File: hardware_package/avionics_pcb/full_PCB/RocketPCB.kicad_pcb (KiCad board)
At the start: 2 copper layers, 0.8 x 1 mm, 72 parts, among them J1 DX07S024XJ1R1100, J2 Micro_SD_Card, J3 Conn_01x03_Female, M1 Motor_Servo_JR, M2 Motor_Servo_JR, Q1 DMG2301L, Q2 DMG2301L, SW1 SW_Push, SW2 SW_Push, U1 STM32F405RGTx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

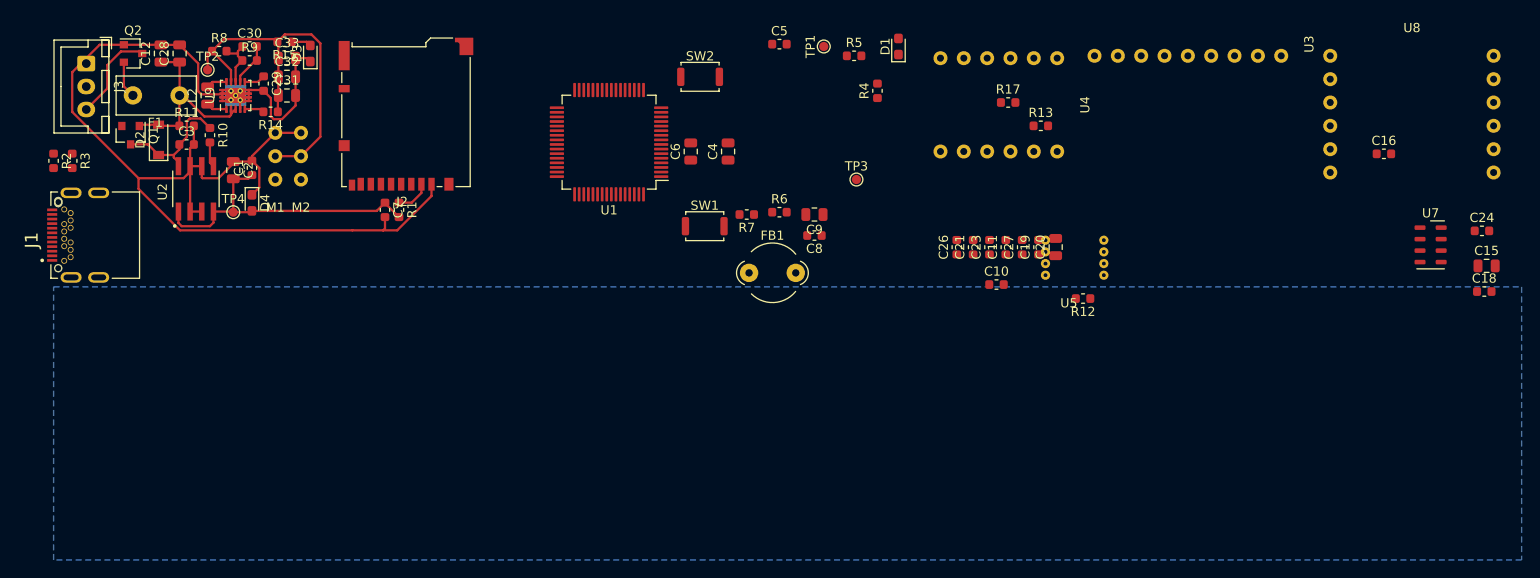
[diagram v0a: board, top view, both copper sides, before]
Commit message: Laid out and routed the majority of the board
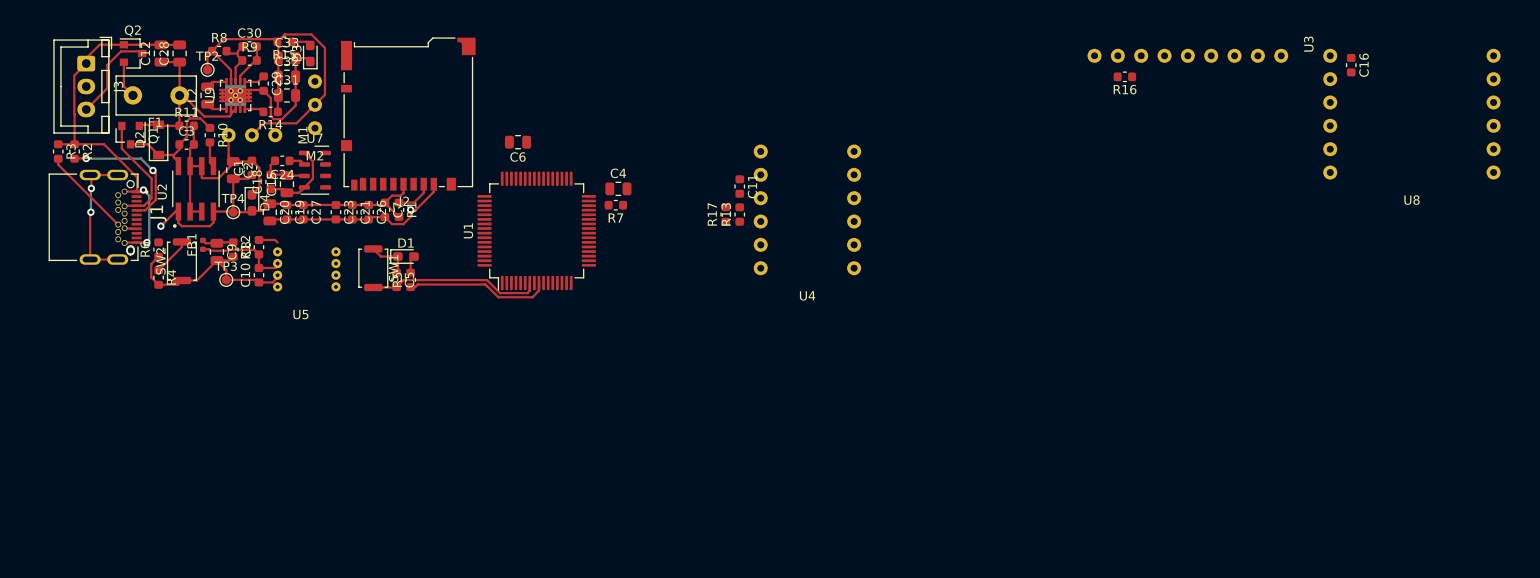
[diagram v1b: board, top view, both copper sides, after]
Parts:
- removed TP1: TestPoint, TestPoint:TestPoint_Pad_D1.0mm
- added R16: 4.7K, Resistor_SMD:R_0603_1608Metric, F.Cu at (182.6, 59.9)
- C7: value C -> 100nF
- FB1: footprint Ferrite_THT:LairdTech_28C0236-0JW-10 -> Resistor_SMD:R_0402_1005Metric
- moved C18 132.6 mm to (89.7, 71.4), turned to 90 degrees
- moved C15 130.9 mm to (91.4, 71.6), turned to 90 degrees
- moved C24 130.8 mm to (90.9, 69.1), turned to 180 degrees
- moved U7 121.7 mm to (94.5, 70.1)
- moved R12 89.9 mm to (88.4, 78.5), turned to 90 degrees
- moved C20 85.6 mm to (89.6, 74.7), turned to 270 degrees
- moved U5 83.6 mm to (93.0, 85.3)
- moved C19 81.9 mm to (91.4, 74.7), turned to 270 degrees
- moved R4 80.8 mm to (77.5, 81.8), turned to 270 degrees
- moved C10 80.3 mm to (88.4, 81.5), turned to 90 degrees
- moved C27 78.3 mm to (93.2, 74.7), turned to 270 degrees
- moved C23 71.2 mm to (96.8, 74.7), turned to 270 degrees
- moved TP3 69.4 mm to (84.8, 82.0)
- moved R6 67.7 mm to (77.5, 78.7), turned to 90 degrees
- moved C21 67.7 mm to (98.6, 74.7), turned to 270 degrees
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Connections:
- net /A0 renamed Net-(U1-Pad20)
- net /CLKIN renamed Net-(U4-Pad8)
- U1 pad 16: /PPS -> Net-(U1-Pad16)
- U1 pad 21: /INT2 -> Net-(U1-Pad21)
- U1 pad 22: /INT1 -> Net-(U1-Pad22)
- U1 pad 23: /INT -> Net-(U1-Pad23)
- U1 pad 26: /CS -> Net-(U1-Pad26)
- U1 pad 39: /SDIO_D0 -> /SDIO_D1
- U1 pad 40: /SDIO_D1 -> /SDIO_D0
- U3 pad 8: /CS -> Net-(R16-Pad2)
- U4 pad 6: /INT -> Net-(U4-Pad6)
- U7 pad 5: /INT2 -> Net-(U7-Pad5)
- U7 pad 6: /INT1 -> Net-(U7-Pad6)
- U8 pad 11: /PPS -> Net-(U8-Pad11)
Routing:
- net +3V3: track 33.7 -> 68.7 mm, vias 0 -> 1
- net ~RESET~: track 0.00 -> 18.9 mm
- net /D13: track 0.00 -> 15.8 mm
- net Net-(J1-PadS1): track 0.00 -> 15.3 mm, vias 0 -> 2
- net Net-(J1-PadA5): track 0.00 -> 15.0 mm, vias 0 -> 2
- net VBUS: track 0.00 -> 13.8 mm
- net GND: track 139.4 -> 149.4 mm, vias 0 -> 3
- net Net-(J1-PadB5): track 0.00 -> 9.87 mm
- net /BOOT0: track 0.00 -> 4.14 mm
- net Net-(C8-Pad1): track 0.00 -> 3.47 mm
- net /FLASH_CS: track 0.00 -> 2.15 mm
- net Net-(D1-Pad2): track 0.00 -> 1.90 mm
- net Net-(C24-Pad1): track 0.00 -> 1.78 mm
- added copper zone on PWR, net +3V3
- added copper zone on GND, net GND
- removed copper zone on B.Cu, net GND
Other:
- copper layers 2 -> 4

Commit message: Continued routing pins, 18 left
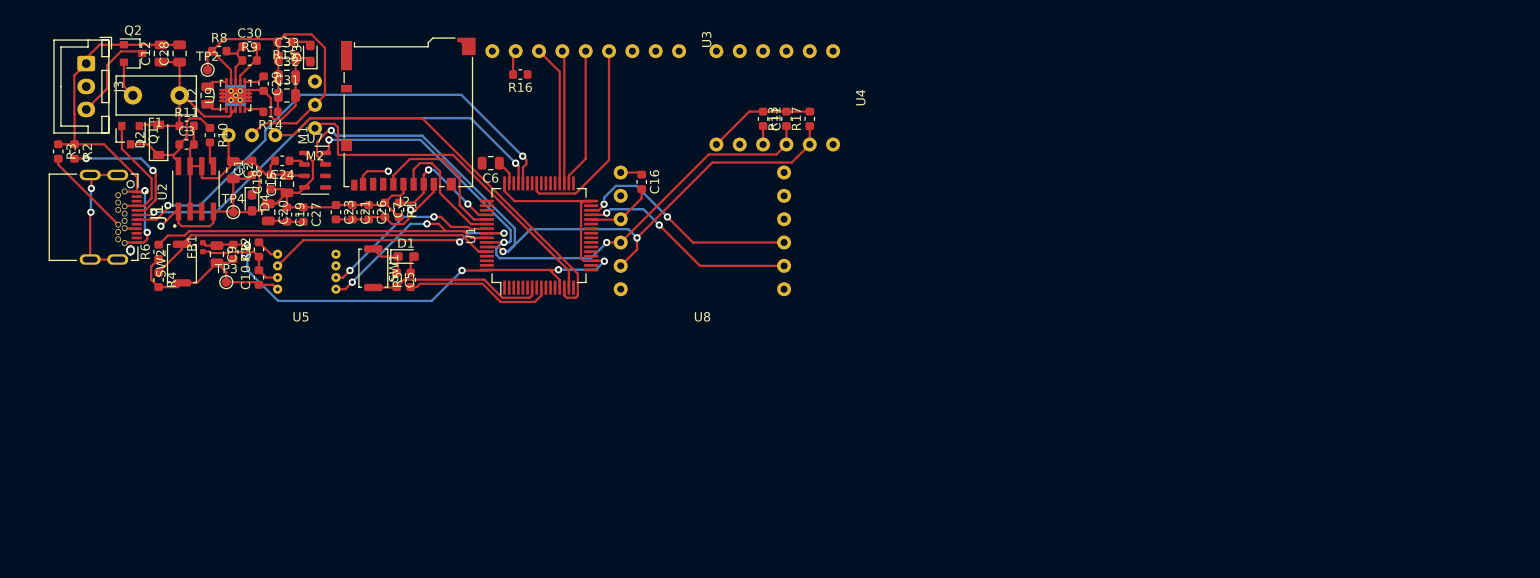
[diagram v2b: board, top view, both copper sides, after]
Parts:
- removed C4: 10uF, Capacitor_SMD:C_0805_2012Metric
- removed R7: 100k, Resistor_SMD:R_0603_1608Metric
- moved C16 78.3 mm to (130.0, 71.4)
- moved U8 78.3 mm to (136.7, 84.3)
- moved R16 65.8 mm to (116.8, 59.7)
- moved U3 65.5 mm to (135.4, 57.1)
- moved U4 21.7 mm to (153.4, 62.2), turned to 90 degrees
- moved R17 13.9 mm to (148.3, 64.5)
- moved R13 11.6 mm to (145.8, 64.5)
- moved C11 7.79 mm to (143.3, 64.5)
- moved C6 3.75 mm to (113.6, 69.3)
- moved U1 0.57 mm to (118.9, 77.2)
- moved C19 0.25 mm to (91.4, 74.9)
- moved C27 0.25 mm to (93.2, 74.9)
- moved C8 0.25 mm to (85.6, 79.0)
- moved C9 0.25 mm to (83.8, 79.2)
- moved FB1 0.25 mm to (82.3, 78.5)
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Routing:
- net /SDA: track 0.00 -> 78.8 mm, vias 0 -> 3
- net /SCL: track 0.00 -> 69.9 mm, vias 0 -> 3
- net Net-(C8-Pad1): track 3.47 -> 72.7 mm, vias 0 -> 4
- net /D-: track 0.00 -> 54.5 mm, vias 0 -> 2
- net /FLASH_MOSI: track 0.00 -> 51.9 mm, vias 0 -> 2
- net /D+: track 0.00 -> 50.0 mm, vias 0 -> 2
- net /PWM0: track 0.00 -> 45.6 mm
- net /PWM1: track 0.00 -> 38.0 mm
- net /BOOT0: track 4.14 -> 38.5 mm
- net /FLASH_MISO: track 0.00 -> 28.1 mm, vias 0 -> 2
- net /RX_D0: track 0.00 -> 25.1 mm, vias 0 -> 2
- net /TX_D1: track 0.00 -> 23.8 mm, vias 0 -> 2
- net /G0: track 0.00 -> 22.2 mm
- net /FLASH_SCK: track 0.00 -> 19.7 mm, vias 0 -> 2
- net +3V3: track 68.7 -> 85.3 mm
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
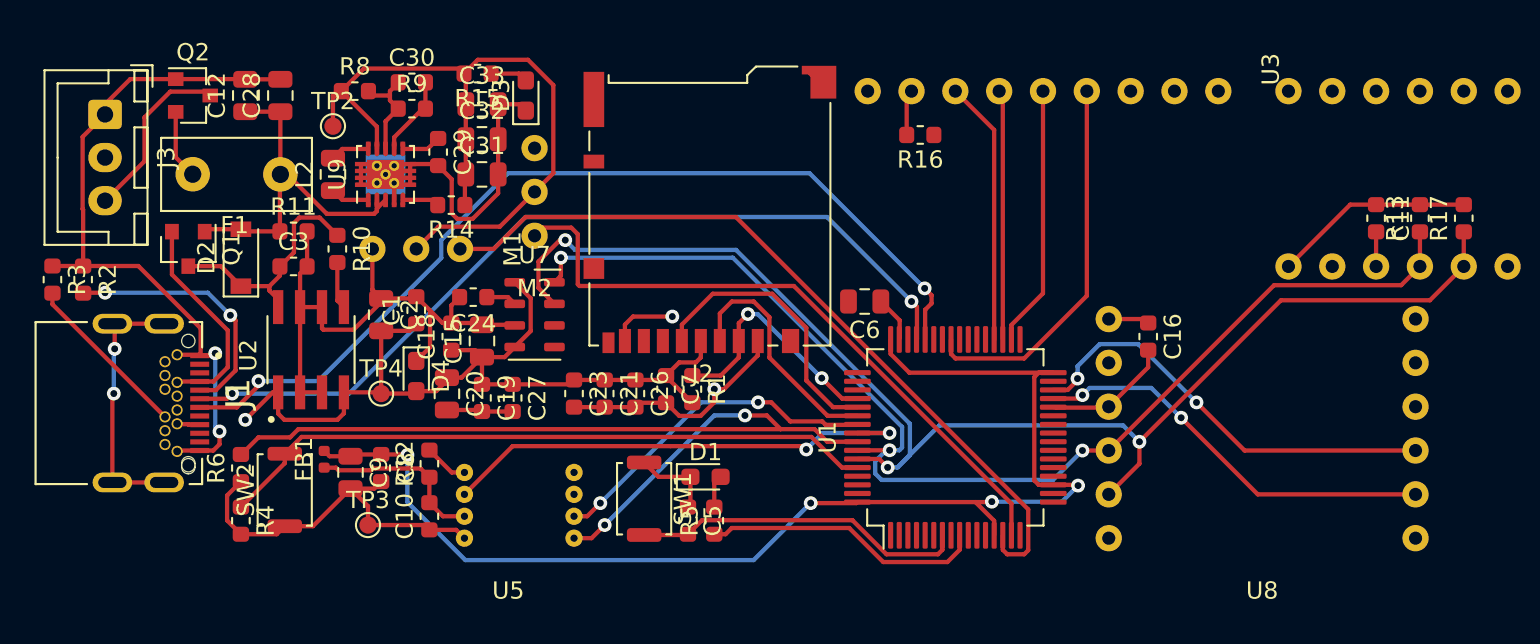
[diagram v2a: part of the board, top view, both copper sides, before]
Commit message: Finished routing and laying out first iteration of final PCB
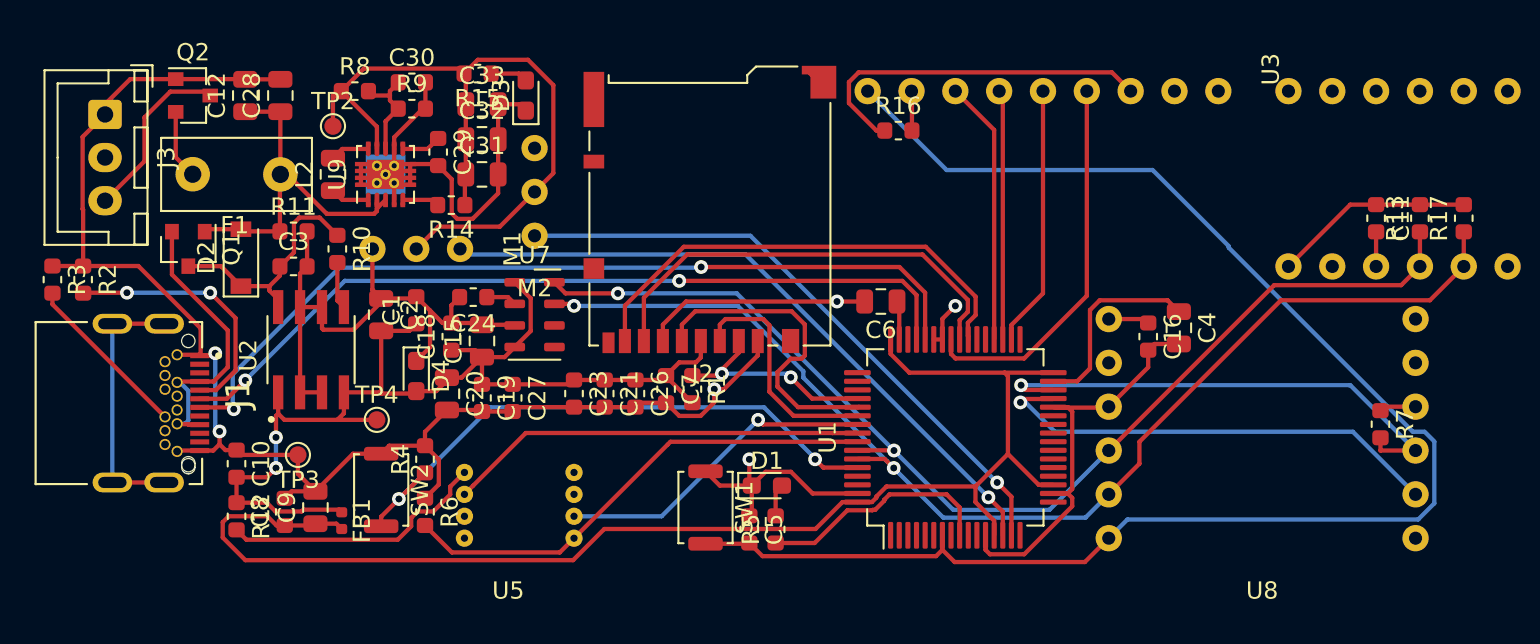
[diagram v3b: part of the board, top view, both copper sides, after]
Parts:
- added C4: 10uF, Capacitor_SMD:C_0805_2012Metric, F.Cu at (131.8, 70.9)
- added R7: 100k, Resistor_SMD:R_0603_1608Metric, F.Cu at (143.5, 76.5)
- moved C10 11.6 mm to (77.2, 78.7), turned to 270 degrees
- moved R12 11.6 mm to (77.2, 81.8), turned to 270 degrees
- moved R4 11.2 mm to (88.1, 78.5), turned to 90 degrees
- moved R6 11.0 mm to (88.1, 81.5), turned to 270 degrees
- moved C8 6.14 mm to (80.0, 81.5), turned to 90 degrees
- moved TP3 5.75 mm to (80.8, 78.2), turned to 180 degrees
- moved SW2 5.59 mm to (85.6, 80.3), turned to 270 degrees
- moved FB1 3.70 mm to (83.3, 82.0), turned to 270 degrees
- moved SW1 3.59 mm to (104.4, 81.3)
- moved D1 3.59 mm to (108.0, 80.0)
- moved C5 3.59 mm to (106.9, 82.5)
- moved R5 3.59 mm to (108.5, 82.5)
- moved C9 2.87 mm to (81.8, 81.3), turned to 90 degrees
- moved TP4 1.55 mm to (85.3, 76.2)
- moved R16 1.30 mm to (115.6, 59.4), turned to 0 degrees
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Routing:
- net ~RESET~: track 19.4 -> 90.1 mm
- net GND: track 156.5 -> 201.3 mm, vias 3 -> 5
- net +3V3: track 85.3 -> 114.2 mm, vias 1 -> 3
- net /SDIO_D0: track 0.00 -> 25.9 mm
- net /SDIO_D1: track 3.89 -> 27.7 mm, vias 1 -> 0
- net /FLASH_MOSI: track 51.9 -> 28.4 mm, vias 2 -> 0
- net /FLASH_CS: track 2.57 -> 15.6 mm
- net Net-(C4-Pad1): track 0.00 -> 11.5 mm
- net /SDA: track 78.8 -> 69.1 mm, vias 3 -> 2
- net /PWM0: track 45.6 -> 39.1 mm, vias 0 -> 1
- net Net-(C8-Pad1): track 72.7 -> 79.1 mm, vias 4 -> 0
- net /D-: track 54.5 -> 50.1 mm
- net /SCL: track 69.9 -> 65.6 mm, vias 3 -> 2
- net /BOOT0: track 38.5 -> 34.4 mm, vias 0 -> 2
- net /RX_D0: track 25.1 -> 29.2 mm, vias 2 -> 1
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
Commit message: Minor edit
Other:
- board text added: "Group 3 Avionics PCB"
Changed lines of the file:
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@@
   (general
     (thickness 1.6)
-    (drawings 6)
+    (drawings 7)
     (tracks 589)
     (zones 0)
@@
     )
   )
+  (gr_text "Group 3 Avionics PCB " (at 108.712 82.677) (layer B.Cu)
+    (effects (font (size 1.5 1.5) (thickness 0.3)) (justify mirror))
+  )
   (dimension 88.392365 (width 0.15) (layer Dwgs.User)
